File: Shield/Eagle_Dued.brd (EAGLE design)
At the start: 101.6 x 53.3 mm, 36 parts

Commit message: More updates to schematic for Shield
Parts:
- added IC1: 7805TV, linear:TO220V
- added IC2: LM340MP-05, linear:SOT223
- added JP1: (no value), SparkFun-Connectors:1X04
- added L1: (no value), SparkFun-Passives:INDUCTOR-1206
- added U$1, U$2, U$3, U$4: ACPL-C87A-000E, ck_custom:SO8-WIDE
- added U$5: M24M02-DRMN6TP, ck_custom:SOIC8
- added U$6, U$7: SN65HVD234, ck_custom:SOIC8
- added U$8: DIODE-ZENER-BZT52, SparkFun-DiscreteSemi:SOD-323
- moved D8 185.9 mm to (11.1, 31.3)
- moved C9 164.3 mm to (56.7, 17.5)
- moved C8 163.8 mm to (56.7, 20.2)
- moved C17 163.4 mm to (10.5, 11.1)
- moved C16 156.7 mm to (10.6, 7.42)
- moved C7 156.6 mm to (52.7, 17.6)
- moved C6 155.9 mm to (52.6, 20.1)
- moved C10 148.5 mm to (4.27, 20.7)
- moved C12 148.5 mm to (4.27, 14.0)
- moved C13 148.5 mm to (4.27, 10.7)
- moved C11 148.5 mm to (4.27, 17.4)
- moved C14 148.5 mm to (4.27, 7.32)
- moved C15 148.5 mm to (4.27, 3.96)
- moved C2 138.0 mm to (45.0, 19.9)
- moved C3 138.0 mm to (45.0, 15.8)
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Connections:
- new net N$1: JP1.2, L1.P$1
- new net N$2: D8.A, JP1.1
- new net N$3: D8.C, U$8.1
- net GND: now also L1.P$2, U$8.2

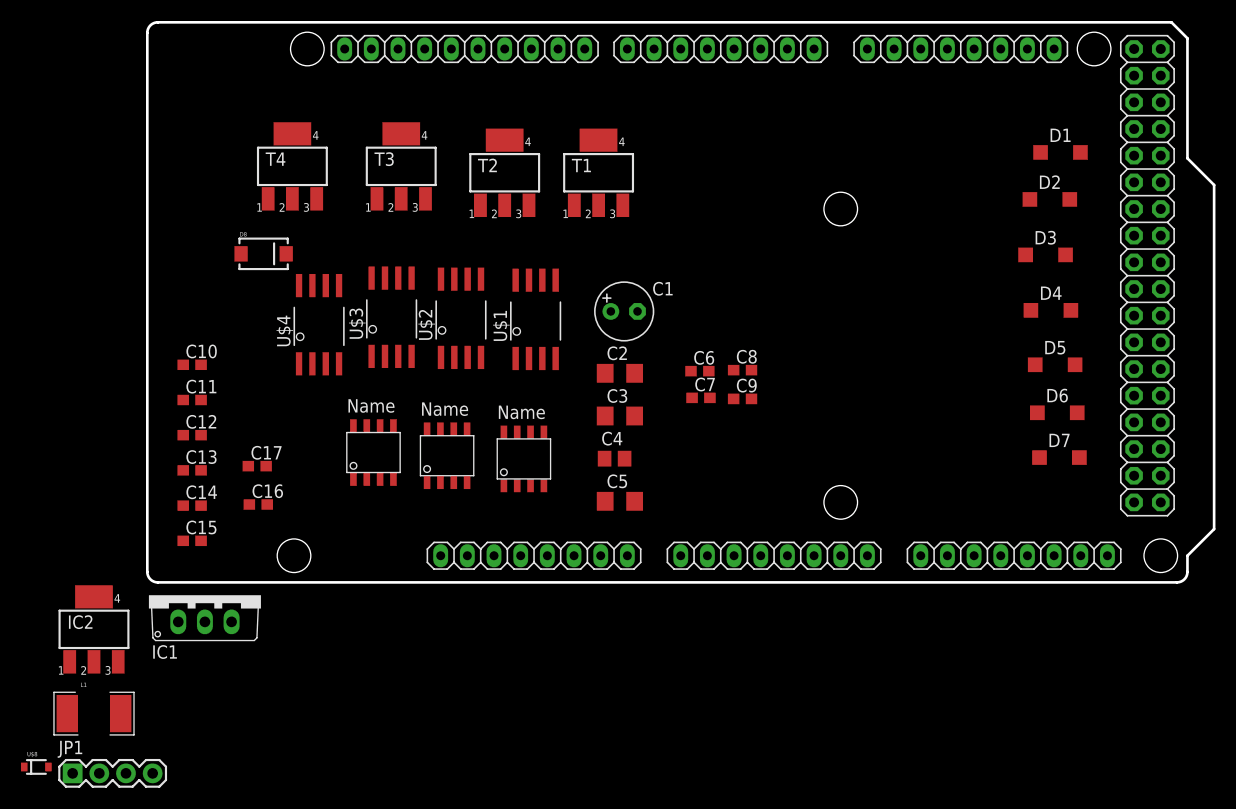
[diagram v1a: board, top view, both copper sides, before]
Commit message: Implemented power section of schematic for shield.
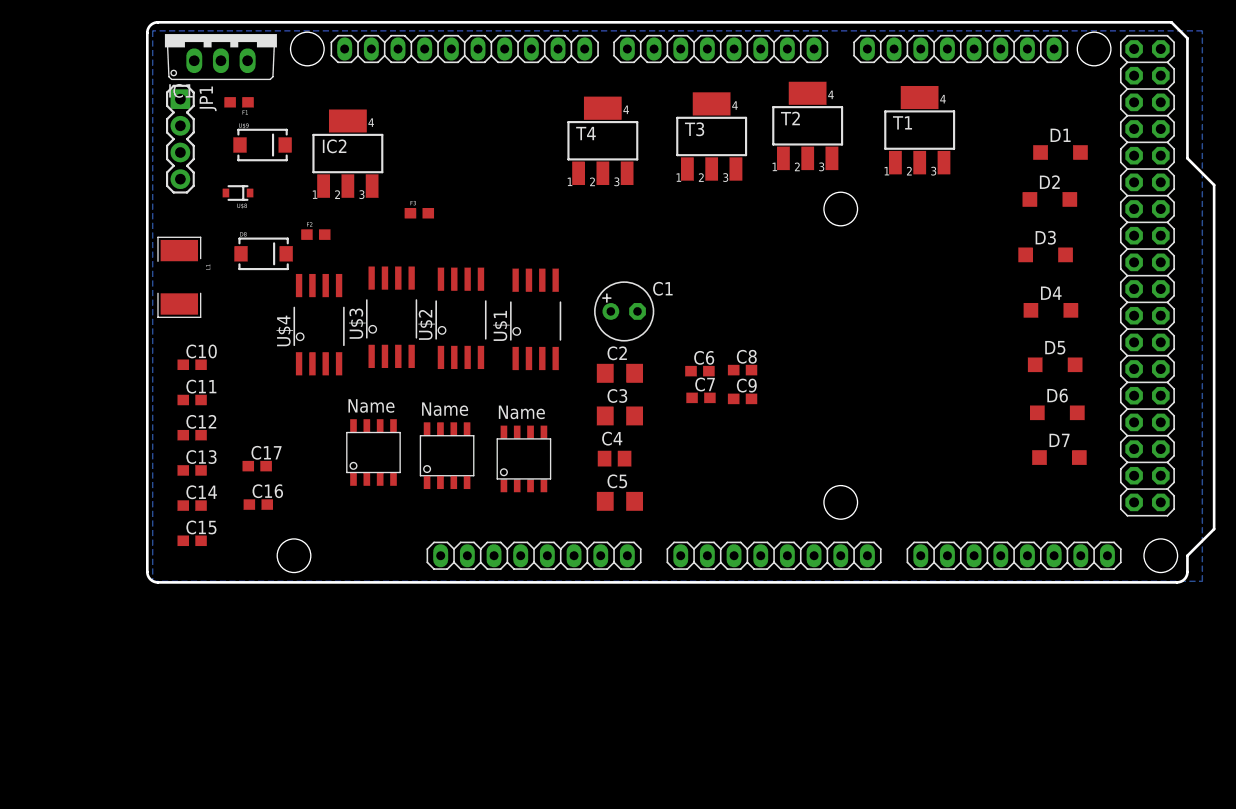
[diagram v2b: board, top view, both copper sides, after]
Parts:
- added F1, F2, F3: PTC0603, SparkFun-PowerIC:0603
- added U$9: TVS, SparkFun-DiscreteSemi:SMA-DIODE
- moved JP1 65.0 mm to (3.15, 46.0), turned to 270 degrees
- moved U$8 57.9 mm to (8.64, 37.1), turned to 180 degrees
- moved IC1 53.5 mm to (7.01, 52.2)
- moved IC2 51.4 mm to (19.1, 40.8)
- moved L1 42.3 mm to (3.05, 29.1), turned to 270 degrees
- moved T1 30.9 mm to (73.6, 43.1)
- moved T3 29.7 mm to (53.7, 42.5)
- moved T4 29.7 mm to (43.4, 42.1)
- moved T2 29.2 mm to (62.9, 43.5)
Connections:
- new net +12V: C1.+, C2.1, C3.1, F1.2, IC1.1
- new net N$6: C4.1, F2.1, IC1.3
- new net N$8: C5.1, F3.1, IC2.3
- net +3V3: now also F3.2
- net +5V: now also F2.2, IC2.1
- net GND: now also C1.-, C2.2, C3.2, C4.2, C5.2, IC1.2, IC2.4, U$9.A
- net N$3: now also F1.1, U$9.C
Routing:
- added copper zone on layer 16, net GND

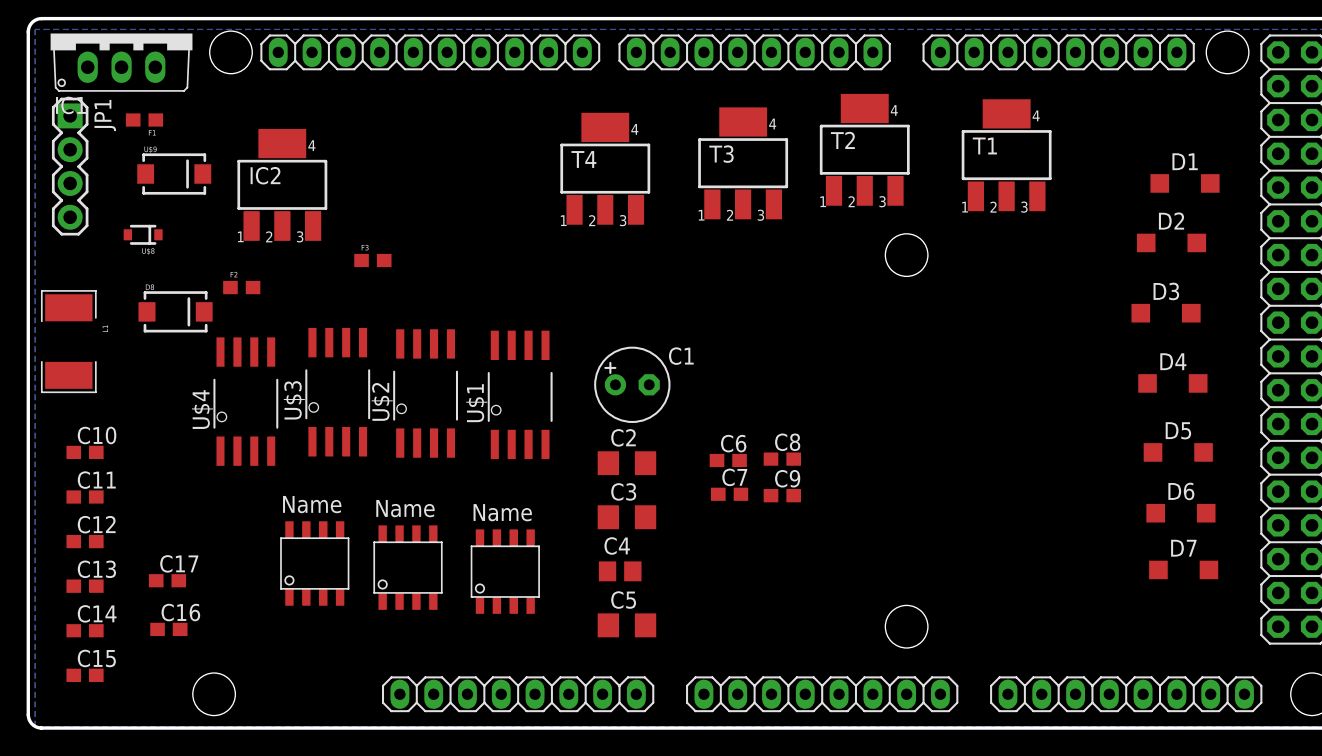
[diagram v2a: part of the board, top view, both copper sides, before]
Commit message: Schematic of DueD basically complete now.
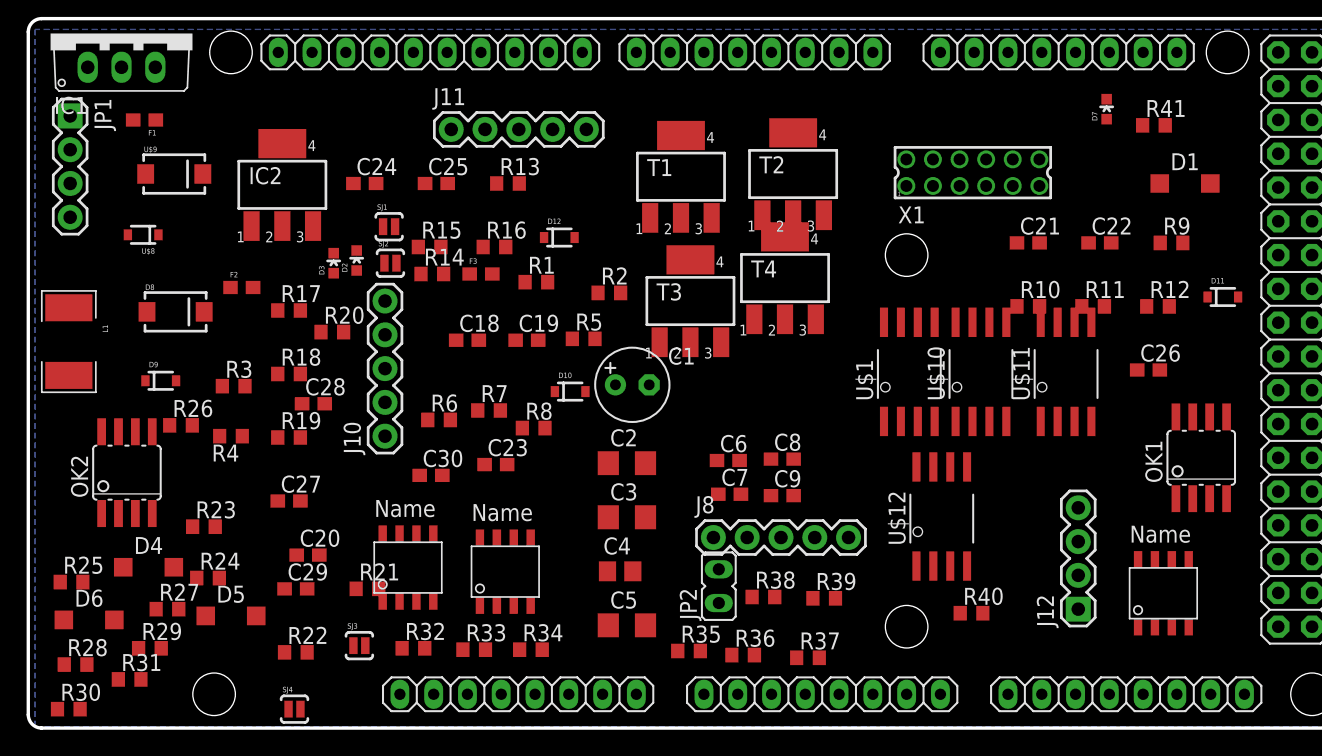
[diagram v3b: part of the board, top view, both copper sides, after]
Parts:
- removed C10, C11, C12, C13, C14, C15, C16, C17: (no value), rcl:C0603
- removed U$3, U$4: ACPL-C87A-000E, ck_custom:SO8-WIDE
- removed U$7: SN65HVD234, ck_custom:SOIC8
- added C18, C19, C21, C22, C24, C25, C27, C29: .1uF, rcl:C0603
- added C20, C23, C26: 100pf, rcl:C0603
- added C28, C30: 47nF, rcl:C0603
- added D10, D11, D12, D9: TVS, SparkFun-DiscreteSemi:SOD-323
- added J10: Analog Inputs, SparkFun-Connectors:1X05
- added J11: MOSFET OUTPUTS, SparkFun-Connectors:1X05
- added J12: CANBUS, SparkFun-Connectors:1X04
- added J8: DIGITAL INPUTS, SparkFun-Connectors:1X05
- added JP2: (no value), jumper:JP1
- added OK1, OK2: ILD213, optocoupler:SOIC08
- added R1, R10, R11, R13, R14, R15, R19, R2, R21, R25, R26, R27, R28, R3, R31, R37, R38, R39, R5, R6, R7, R9: 10K, rcl:R0603
- added R12, R16, R4, R8: 16K, rcl:R0603
- added R17: 510, rcl:R0603
- added R18: 330, rcl:R0603
- added R20, R22: 120, rcl:R0603
- added R23, R24: 4.7K, rcl:R0603
- added R29, R30, R32, R33, R34, R35, R36, R40: 1K, rcl:R0603
- added R41: 33, rcl:R0603
- added SJ1, SJ2, SJ3, SJ4: SOLDERJUMPERNO, SparkFun-Passives:SJ_2S-NO
- added U$10, U$11, U$12: ACPL-C87A-000E, ck_custom:SO8-WIDE
- added X1: 87758-1216, con-molex:87758-1216
- C1: value (none) -> 100uF
- C2: value (none) -> 1uF
- C3, C6, C7: value (none) -> .1uF
- C4: value (none) -> .33uF
- C5: value (none) -> 10uF
- C8: value (none) -> 100pf
- D2, D3, D7: value MBR0520LT -> GREEN; device diode:SOD123 -> SparkFun-LED:LED-0603
- U$2: value ACPL-C87A-000E -> SN65HVD234; device ck_custom:SO8-WIDE -> ck_custom:SOIC8
- moved D6 82.5 mm to (4.57, 8.13)
- moved D4 78.2 mm to (9.04, 12.1)
- moved D5 72.3 mm to (15.2, 8.43)
- moved D3 62.7 mm to (23.0, 35.0)
- moved D2 61.3 mm to (24.7, 35.2)
- moved U$2 57.3 mm to (82.8, 8.23)
- moved D7 35.1 mm to (81.1, 46.5)
- moved U$1 29.3 mm to (63.7, 24.1)
- moved T1 24.5 mm to (49.1, 41.5)
- moved T4 15.8 mm to (56.9, 33.8)
- moved T3 11.1 mm to (49.8, 32.1)
- moved F3 8.19 mm to (34.0, 34.1)
- moved T2 5.69 mm to (57.5, 41.7)
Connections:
- removed net AD11(TXD3): ADCH.4
- removed net AD14(RXD3): XIO.33
- removed net AD8: ADCH.1
- removed net CANTX1/IO: XIO.34
- removed net DAC0(CANRX1): ADCH.5
- removed net PIN22: XIO.3
- removed net PIN32: XIO.13
- removed net PIN48: XIO.29
- removed net RXD0: COMMUNICATION.2
- removed net SCL0-3: COMMUNICATION.8
- removed net SDA0-3: COMMUNICATION.7
- removed net TXD0: COMMUNICATION.1
- new net AIN1: D9.1, J10.1
- new net AIN2: D10.1, J10.2
- new net AIN3: D11.1, J10.3
- new net AIN4: D12.1, J10.4
- new net CAN0-EN: ADCH.1, U$6.PIN5
- new net CAN1-EN: ADCH.4, U$2.PIN5
- new net CANH0: J12.3, SJ1.1, U$6.PIN7
- new net CANH1: J12.2, SJ3.1, U$2.PIN7
- new net CANL0: J12.4, SJ2.1, U$6.PIN6
- new net CANL1: J12.1, SJ4.1, U$2.PIN6
- new net CANRX1: ADCH.5, U$2.PIN4
- new net CANTX1: U$2.PIN1, XIO.34
- new net DIG1: PWMH.2, R30.2, R31.1
- new net DIG2: PWMH.4, R34.2, R37.1
- new net DIG3: PWMH.5, R39.1, R40.2
- new net DIG4: PWMH.6, R35.2, R38.1
- new net DIGOUT1: R25.1, T1.1, XIO.33
- new net DIGOUT2: R26.1, T2.1, XIO.3
- new net DIGOUT3: R27.1, T3.1, XIO.29
- new net DIGOUT4: R28.1, T4.1, XIO.13
- new net DIN1: J8.1, R29.1
- new net DIN2: J8.2, R33.1
- new net DIN3: J8.3, R32.1
- new net DIN4: J8.4, R36.1
- new net MOSFET1: D1.C, J11.2, T1.2, T1.4
- new net MOSFET2: D4.C, J11.3, T2.2, T2.4
- new net MOSFET3: D5.C, J11.4, T3.2, T3.4
- new net MOSFET4: D6.C, J11.5, T4.2, T4.4
- new net N$10: R3.2, R4.1, U$1.2
- new net N$11: R7.2, R8.1, U$10.2
- new net N$12: R5.1, U$10.7
- new net N$13: R6.1, U$10.6
- new net N$14: C20.1, R8.2
- new net N$15: R11.2, R12.1, U$11.2
- new net N$16: R9.1, U$11.7
- new net N$17: R10.1, U$11.6
- new net N$18: C23.1, R12.2
- new net N$19: R15.2, R16.1, U$12.2
- new net N$20: R13.1, U$12.7
- new net N$21: R14.1, U$12.6
- new net N$22: C26.1, R16.2
- new net N$23: D2.A, R17.2
- new net N$24: R19.2, U$6.PIN8
- new net N$25: D3.A, R18.2
- new net N$26: C28.1, R20.1, SJ2.2
- new net N$27: R20.2, SJ1.2
- new net N$28: R21.2, U$2.PIN8
- new net N$29: C30.1, R22.1, SJ4.2
- new net N$30: R22.2, SJ3.2
- new net N$31: OK1.1, R29.2
- new net N$32: OK1.3, R33.2
- new net N$33: OK1.8, R30.1
- new net N$34: OK1.6, R34.1
- new net N$35: X1.5, X1.7
- new net N$36: OK2.6, R35.1
- new net N$37: D7.A, R41.1
- new net N$38: OK2.8, R40.1
- new net N$39: R41.2, X1.12
- new net N$4: JP1.3, JP2.1
- new net N$40: OK2.1, R32.2
- new net N$43: OK2.3, R36.2
- new net N$5: R1.1, U$1.7
- new net N$7: R2.1, U$1.6
- new net N$9: C8.1, R4.2
- new net RXD3: COMMUNICATION.7, X1.4
- new net SCL: COMMUNICATION.1, R23.2, U$5.PIN6
- new net SDA: COMMUNICATION.2, R24.2, U$5.PIN5
- new net TXD3: COMMUNICATION.8, X1.3
- net +3V3: now also C27.1, C29.1, C9.1, R18.1, R23.1, R24.1, R31.2, R37.2, R38.2, R39.2, U$2.PIN3, U$5.PIN8, U$6.PIN3, X1.1
- net +5V: now also C18.1, C19.1, C21.1, C22.1, C24.1, C25.1, C6.1, C7.1, JP1.4, R17.1, U$1.1, U$1.8, U$10.1, U$10.8, U$11.1, U$11.8, U$12.1, U$12.8
- net AD0: now also R1.2
- net AD1: now also R2.2
- net AD2: now also R5.2
- net AD3: now also R6.2
- net AD4: now also R9.2
- net AD5: now also R10.2
- net AD6: now also R13.2
- net AD7: now also R14.2
- net CANRX0: now also U$6.PIN4
- net CANTX0: now also U$6.PIN1
- net GND: now also C18.2, C19.2, C20.2, C21.2, C22.2, C23.2, C24.2, C25.2, C26.2, C27.2, C28.2, C29.2, C30.2, C6.2, C7.2, C8.2, C9.2, D1.A, D10.2, D11.2, D12.2, D2.C, D3.C, D4.A, D5.A, D6.A, D7.C, D9.2, J10.5, J11.1, J8.5, OK1.2, OK1.4, OK1.5, OK1.7, OK2.2, OK2.4, OK2.5, OK2.7, R11.1, R15.1, R19.1, R21.1, R25.2, R26.2, R27.2, R28.2, R3.1, R7.1, T1.3, T2.3, T3.3, T4.3, U$1.3, U$1.4, U$1.5, U$10.3, U$10.4, U$10.5, U$11.3, U$11.4, U$11.5, U$12.3, U$12.4, U$12.5, U$2.PIN2, U$5.PIN1, U$5.PIN2, U$5.PIN3, U$5.PIN4, U$6.PIN2, X1.2
- net RXD1: now also U$5.PIN7
- net RXD2: now also X1.10
- net VIN: now also JP2.2

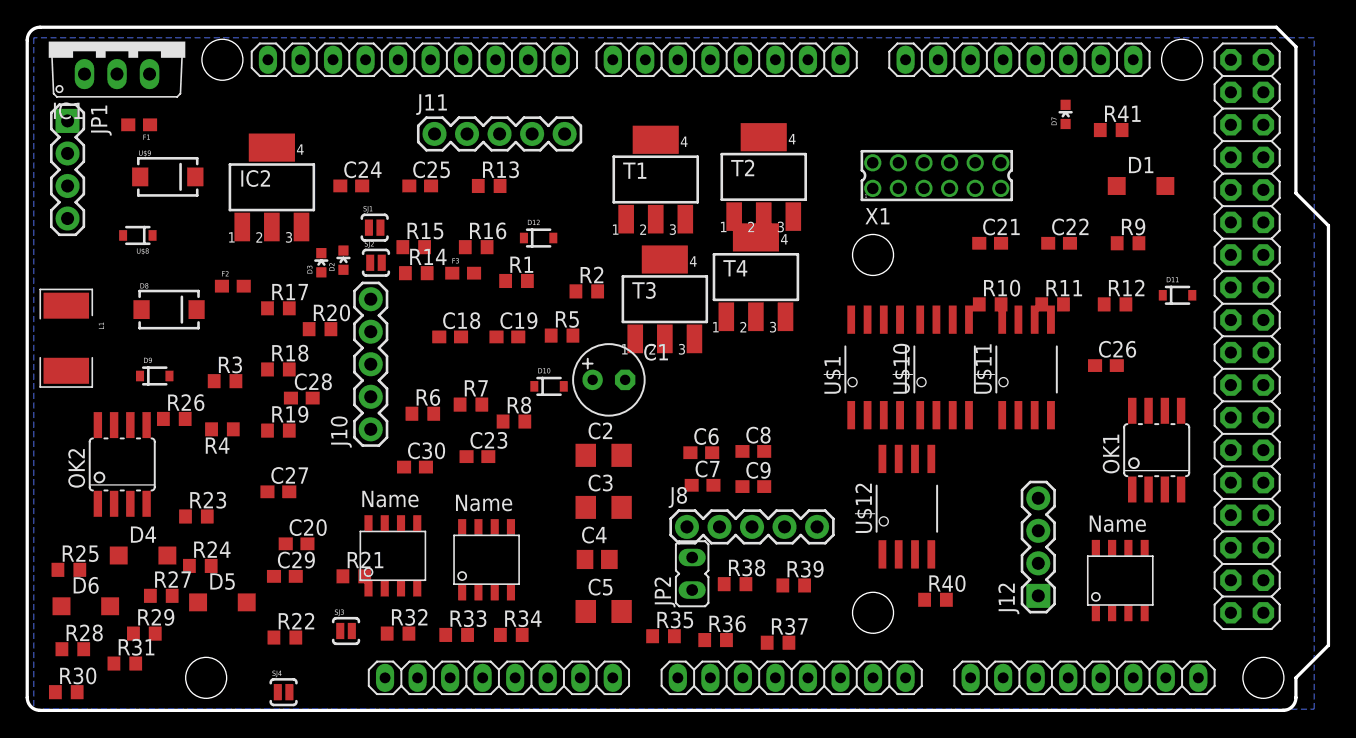
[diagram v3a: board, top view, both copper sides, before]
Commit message: Fixed a couple of errors in the schematic
Placed all parts on board approximately where they'll end up
(in theory)
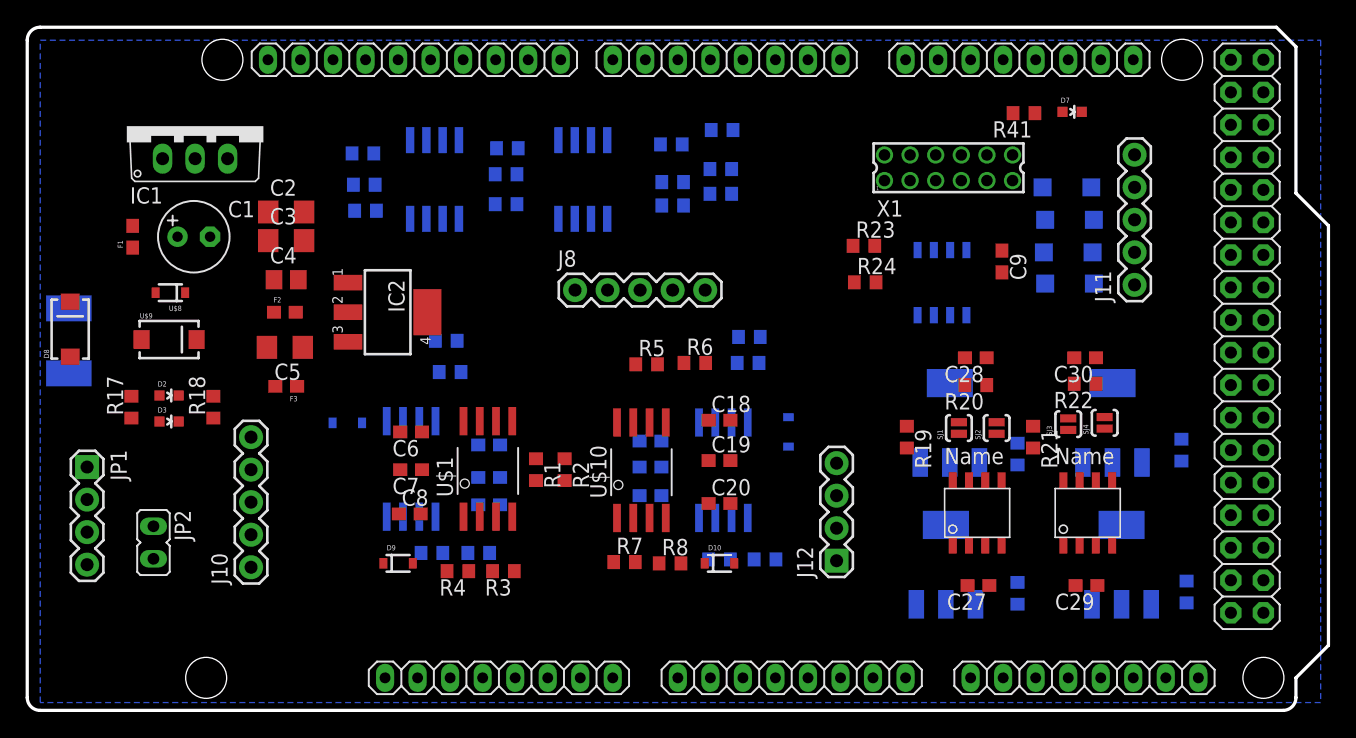
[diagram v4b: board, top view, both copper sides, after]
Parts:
- moved R28 87.9 mm to (90.1, 20.3), flipped to the bottom, turned to 90 degrees
- moved D6 80.8 mm to (81.4, 33.3), flipped to the bottom, turned to 180 degrees
- moved R26 80.2 mm to (90.5, 9.25), flipped to the bottom, turned to 90 degrees
- moved D4 76.9 mm to (81.4, 38.3), flipped to the bottom
- moved R25 74.1 mm to (77.3, 9.14), flipped to the bottom, turned to 90 degrees
- moved D5 73.5 mm to (81.2, 40.8), flipped to the bottom
- moved R27 67.8 mm to (77.3, 20.0), flipped to the bottom, turned to 90 degrees
- moved SJ4 67.5 mm to (84.1, 22.5), turned to 90 degrees
- moved D11 65.6 mm to (25.0, 22.5), flipped to the bottom, turned to 180 degrees
- moved R22 65.5 mm to (82.6, 25.5), turned to 180 degrees
- moved C29 62.6 mm to (82.7, 9.75), turned to 180 degrees
- moved R30 61.9 mm to (50.4, 41.2), flipped to the bottom
- moved SJ3 58.7 mm to (81.3, 22.4), turned to 90 degrees
- moved R24 56.4 mm to (65.4, 33.4)
- moved R23 56.2 mm to (65.3, 36.3)
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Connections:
- removed net N$14: C20.1, R8.2
- removed net N$18: C23.1, R12.2
- removed net N$22: C26.1, R16.2
- removed net N$9: C8.1, R4.2
- net AIN1: now also C8.1, R4.2
- net AIN2: now also C20.1, R8.2
- net AIN3: now also C23.1, R12.2
- net AIN4: now also C26.1, R16.2
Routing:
- added copper zone on layer 16, net N$41
- removed copper zone on layer 16, net GND

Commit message: More board layout and set up
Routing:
- added copper zone on layer 2, net +3V3
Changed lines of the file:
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@@
 <contactref element="R37" pad="2"/>
 <contactref element="X1" pad="1"/>
+<polygon width="0.4064" layer="2">
+<vertex x="0.9144" y="52.4256"/>
+<vertex x="99.06" y="52.4256"/>
+<vertex x="99.06" y="0.6096"/>
+<vertex x="0.9144" y="0.6096"/>
+</polygon>
 <wire x1="73.3298" y1="35.941" x2="76.0984" y2="35.902" width="0" layer="19" extent="1-16"/>
 <wire x1="66.9328" y1="41.3672" x2="73.3298" y2="35.941" width="0" layer="19" extent="16-16"/>
@@
 <wire x1="83.5524" y1="9.7536" x2="75.1196" y2="9.7536" width="0" layer="19" extent="1-1"/>
 <wire x1="83.439" y1="12.8778" x2="83.5524" y2="9.7536" width="0" layer="19" extent="1-1"/>
-<wire x1="30.48" y1="2.54" x2="19.3684" y2="25.2984" width="0" layer="19" extent="1-1"/>
-<wire x1="35.56" y1="2.54" x2="30.48" y2="2.54" width="0" layer="19" extent="1-1"/>
 </signal>
 <signal name="PIN51">
